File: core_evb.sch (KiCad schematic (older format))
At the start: 0 parts

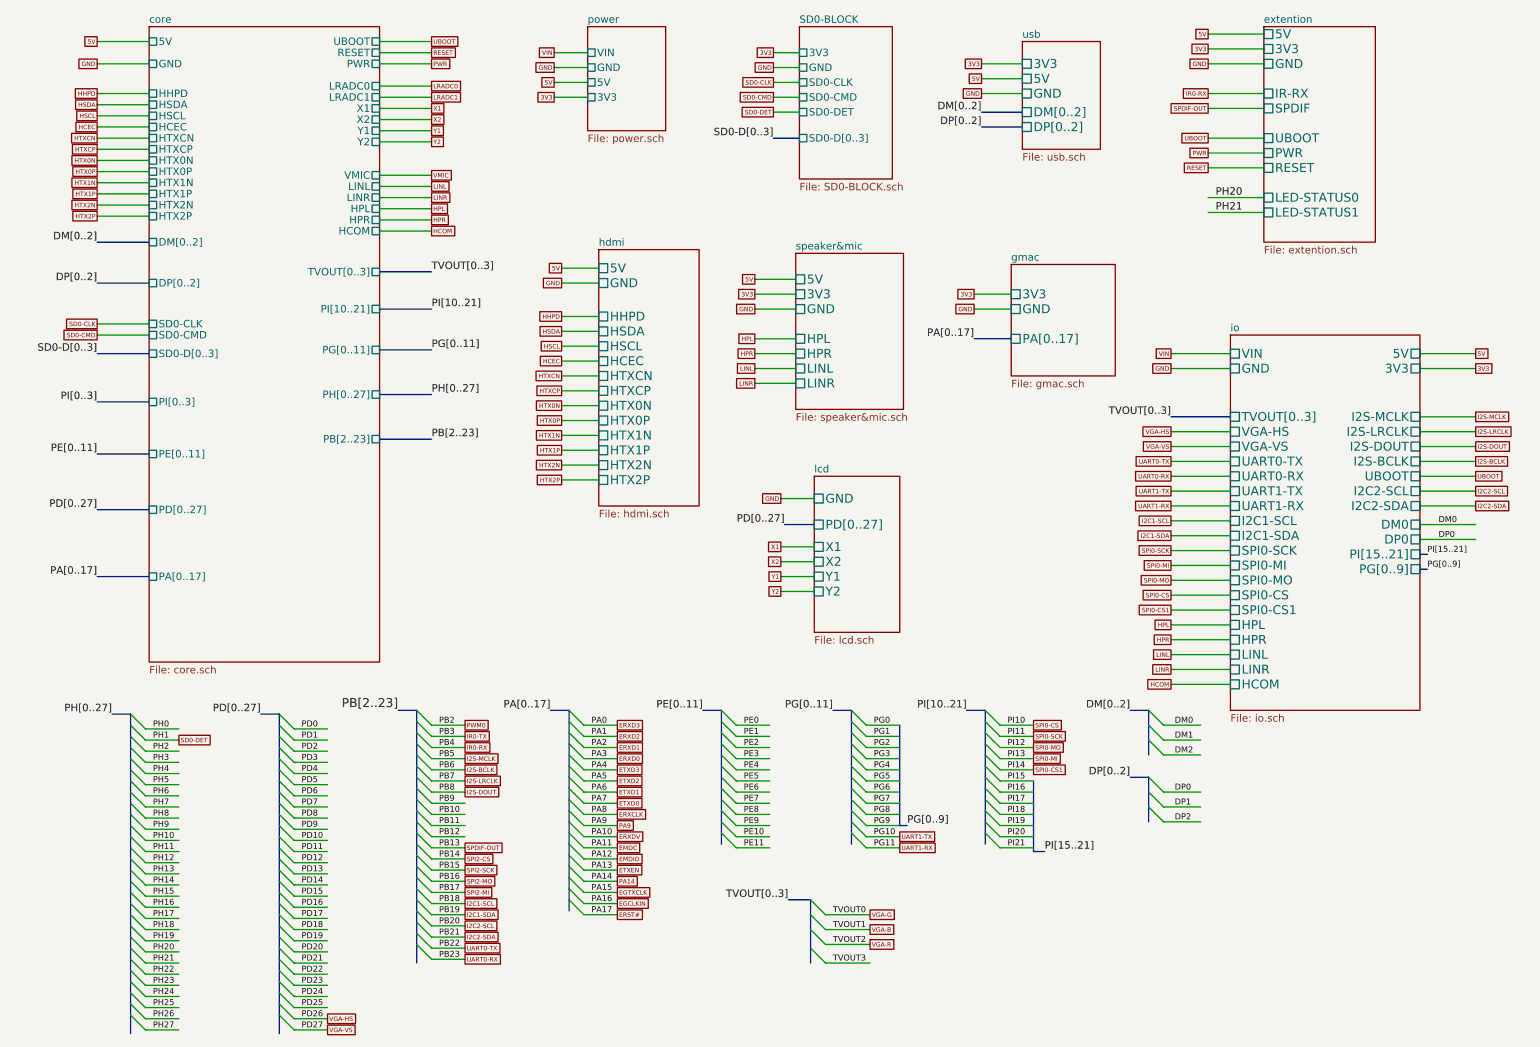
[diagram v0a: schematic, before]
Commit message: 1.4
Fix some issues
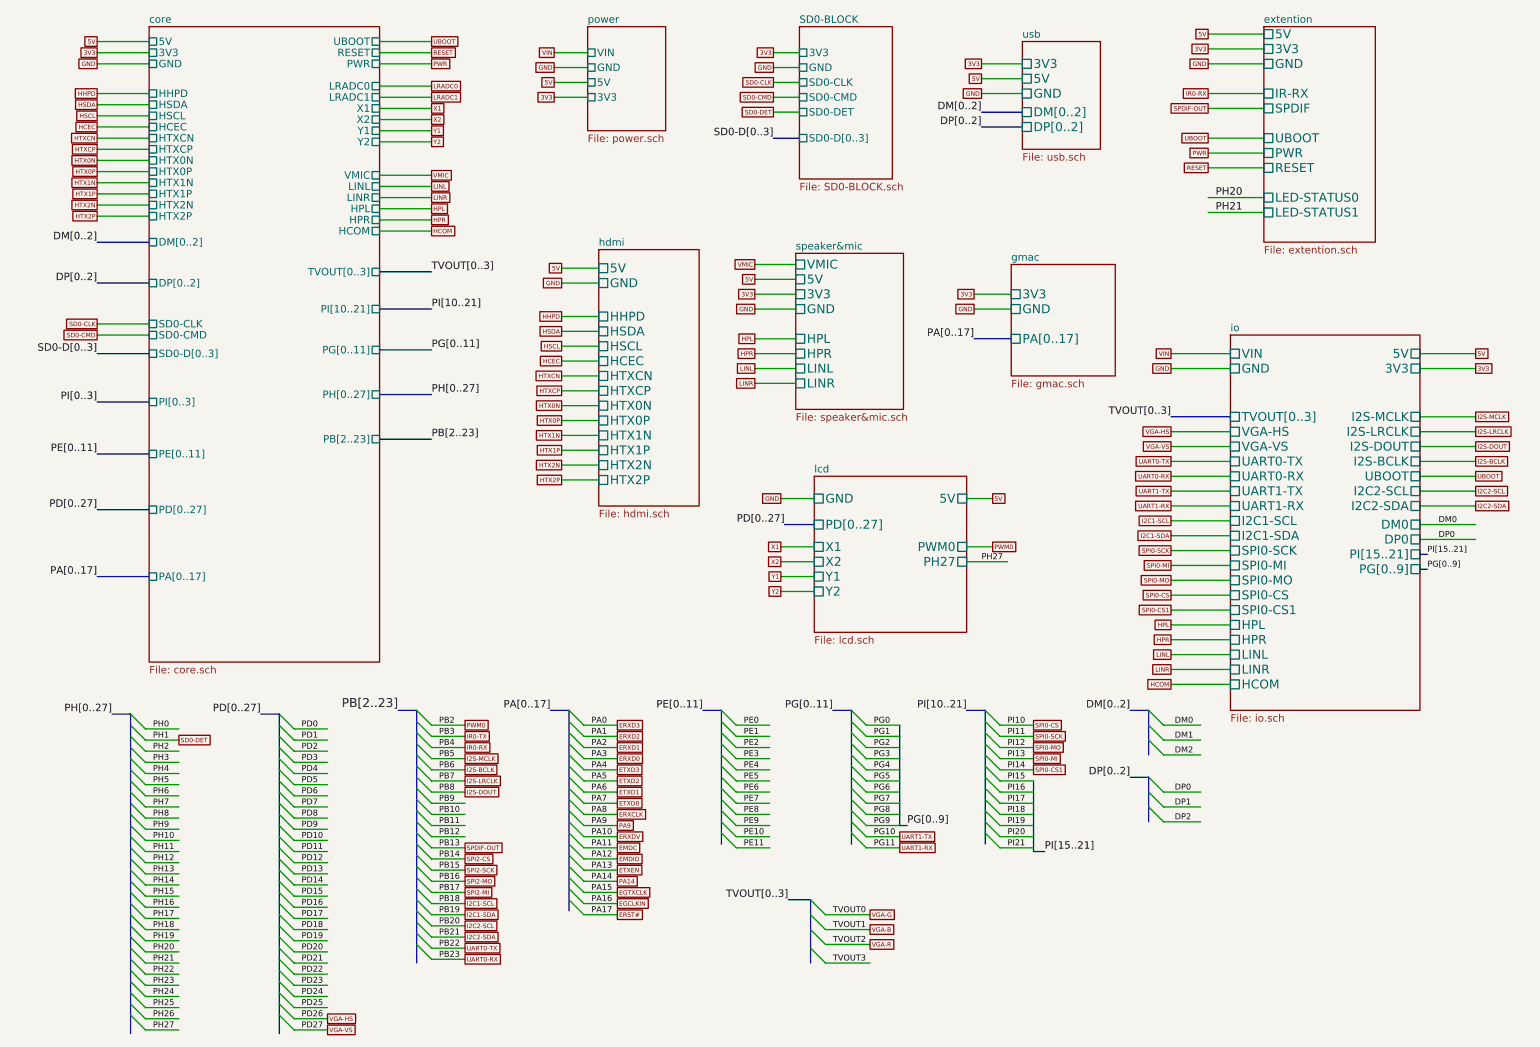
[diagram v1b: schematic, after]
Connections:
- wire segments 254 -> 259
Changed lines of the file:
@@
 Sheet 1 11
 Title "Core EVB"
-Date "19 sep 2014"
+Date "25 nov 2014"
 Rev "V1.0"
 Comp "Itead studio"
@@
 F43 "PH[0..27]" U R 3050 3325 50
 F44 "PB[2..23]" U R 3050 3625 50
+F45 "3V3" U L 1500 1025 50
 $EndSheet
 Text GLabel 1150 950  0    30   UnSpc ~ 0
@@
 F7 "LINL" U L 5850 3150 60
 F8 "LINR" U L 5850 3250 60
+F9 "VMIC" U L 5850 2450 60
 $EndSheet
 Text GLabel 5575 3150 0    30   UnSpc ~ 0
@@
 	5575 3250 5850 3250
 $Sheet
-S 5975 3875 575  1050
+S 5975 3875 1025 1050
 U 53E58617
 F0 "lcd" 50
@@
 F6 "Y1" U L 5975 4550 60
 F7 "Y2" U L 5975 4650 60
+F8 "PWM0" U R 7000 4350 60
+F9 "PH27" U R 7000 4450 60
+F10 "5V" U R 7000 4025 60
 $EndSheet
 Text GLabel 5750 4025 0    30   UnSpc ~ 0
@@
 Wire Wire Line
 	7375 1300 7100 1300
+Text GLabel 1150 1025 0    30   UnSpc ~ 0
+3V3
+Wire Wire Line
+	1500 1025 1150 1025
+Text GLabel 7175 4025 2    30   UnSpc ~ 0
+5V
+Text GLabel 7175 4350 2    30   UnSpc ~ 0
+PWM0
+Wire Wire Line
+	7000 4350 7175 4350
+Wire Wire Line
+	7000 4025 7175 4025
+Text GLabel 5575 2450 0    30   UnSpc ~ 0
+VMIC
+Wire Wire Line
+	5575 2450 5850 2450
+Wire Wire Line
+	7000 4450 7275 4450
+Text Label 7100 4450 0    40   ~ 0
+PH27
 $EndSCHEMATC
